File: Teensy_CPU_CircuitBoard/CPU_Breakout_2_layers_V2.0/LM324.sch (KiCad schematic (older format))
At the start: 44 parts

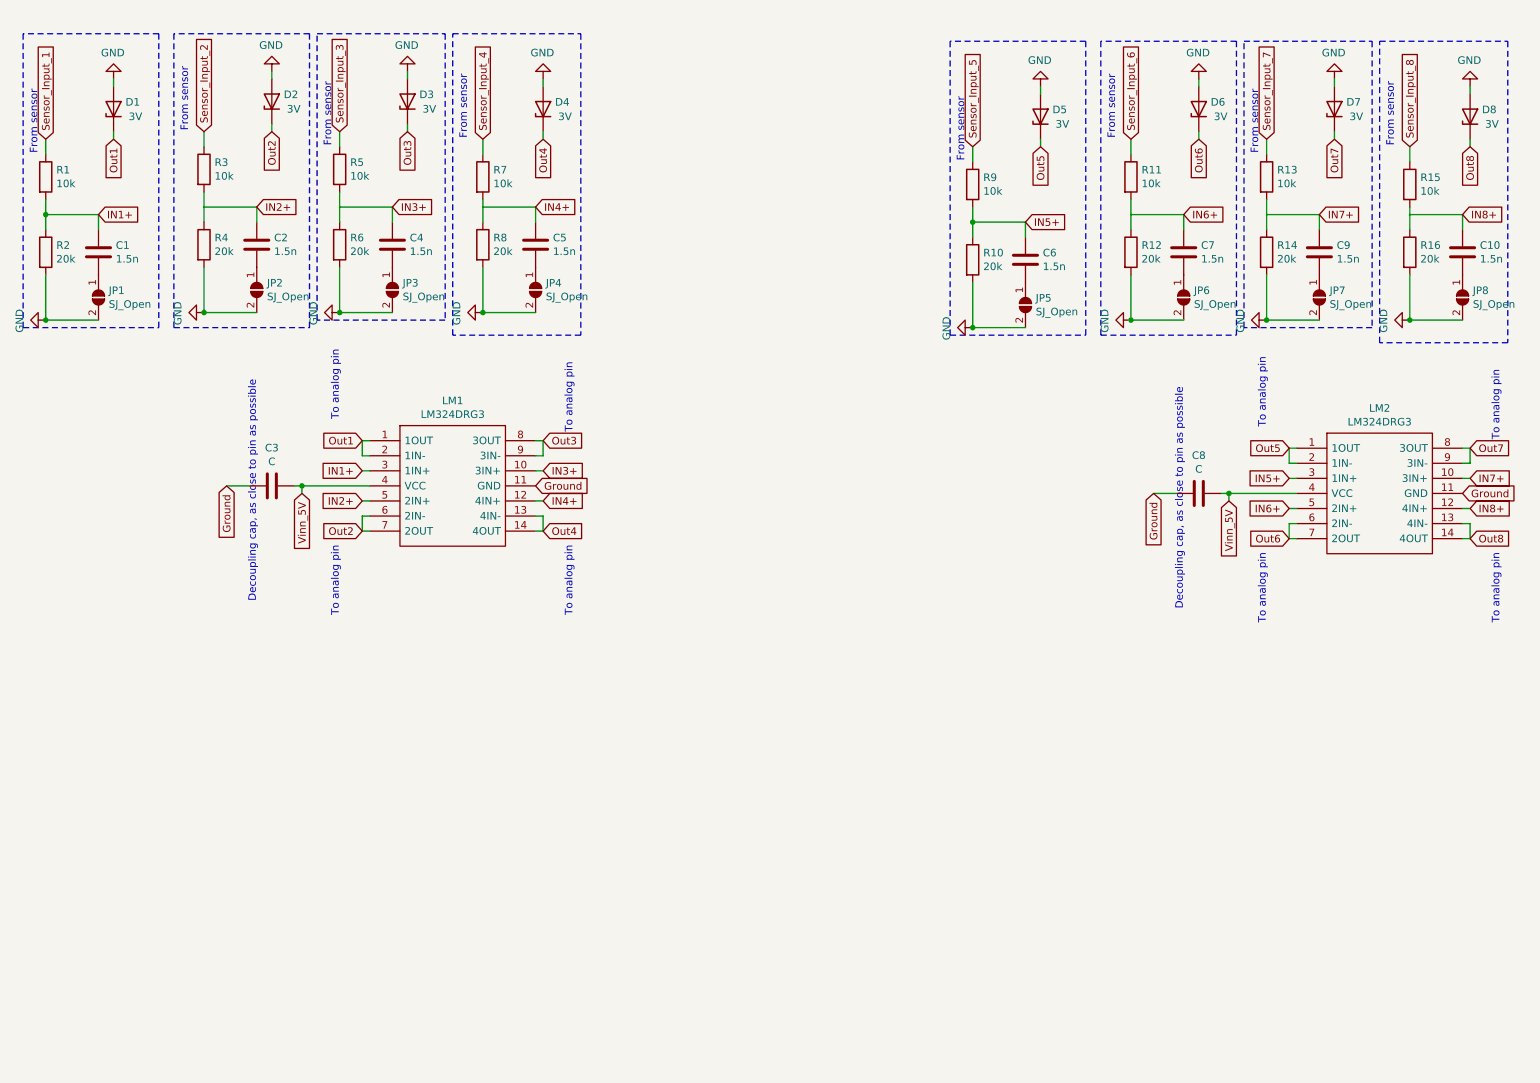
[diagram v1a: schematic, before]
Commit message: Suspension disp senson schematic done
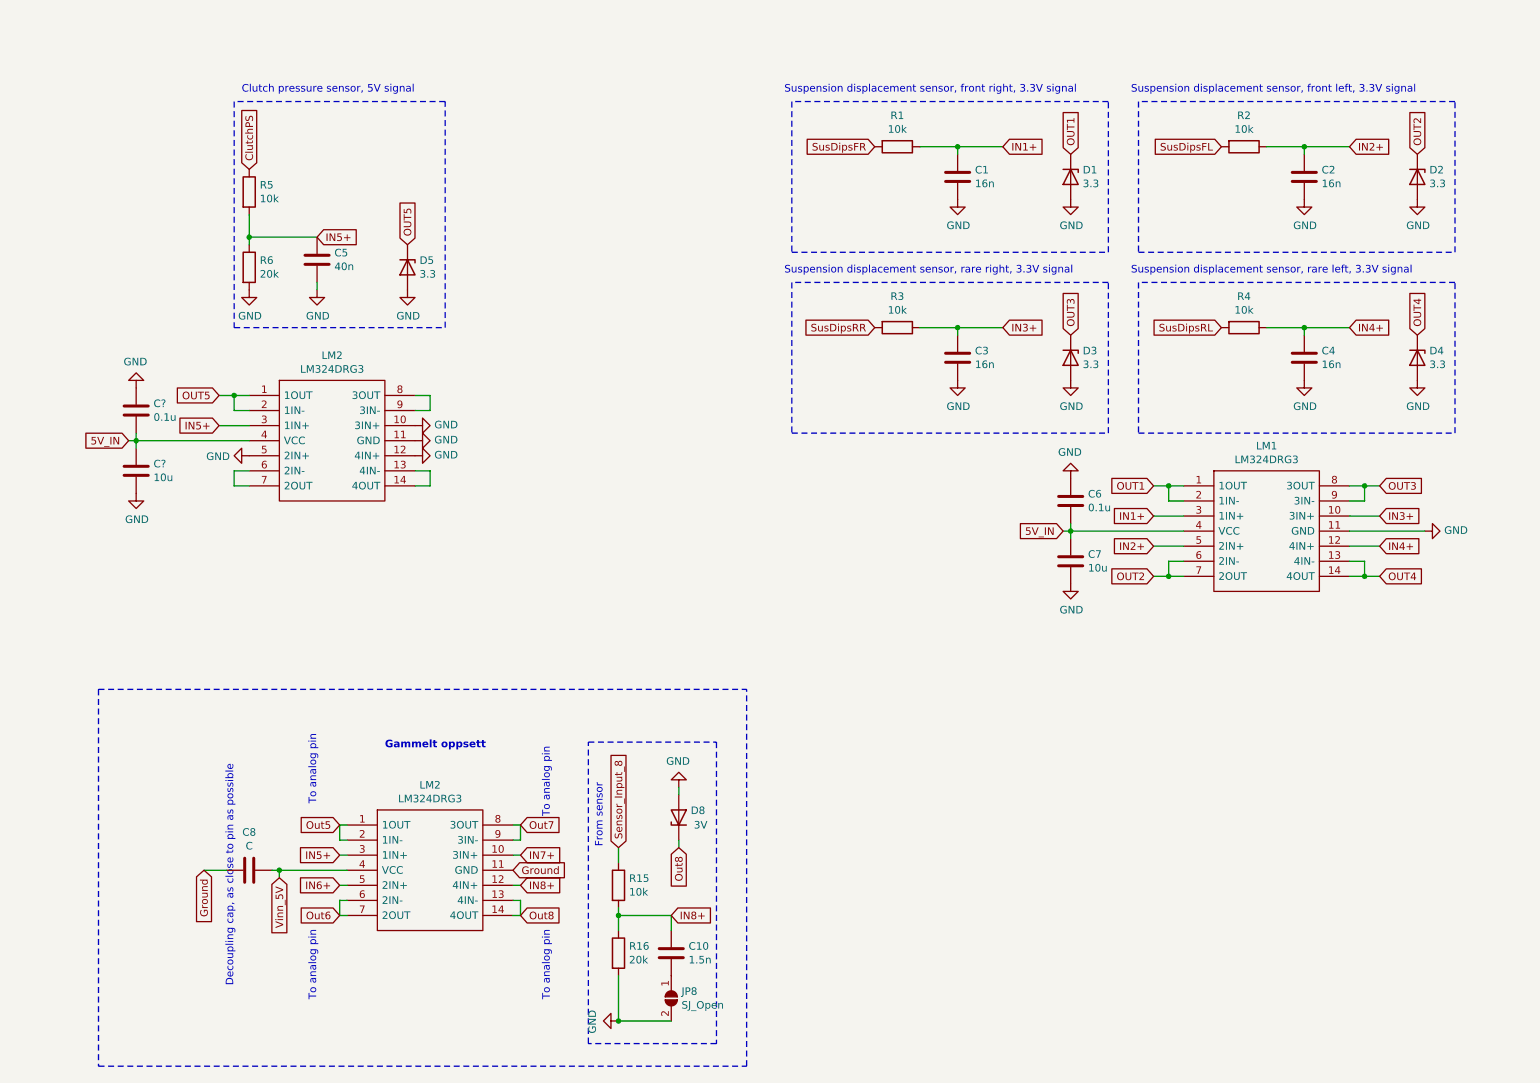
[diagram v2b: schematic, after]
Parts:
- removed C9: 1.5n, Capacitor_SMD:C_0603_1608Metric, symbol Device:C
- removed D6, D7: 3V, Diode_SMD:D_0603_1608Metric, symbol Device:D_Zener
- removed JP1, JP2, JP3, JP4, JP5, JP6, JP7: SJ_Open, Jumper:SolderJumper-2_P1.3mm_Open_RoundedPad1.0x1.5mm, symbol Jumper:SolderJumper_2_Open
- removed R10, R12, R14, R8: 20k, Resistor_SMD:R_0603_1608Metric, symbol Device:R
- removed R11, R13, R7, R9: 10k, Resistor_SMD:R_0603_1608Metric, symbol Device:R
- added C?: 10u, Capacitor_SMD:C_0603_1608Metric, symbol Device:C
- added C?: 0.1u, Capacitor_SMD:C_0603_1608Metric, symbol Device:C
- added LM2: LM324DRG3, Package_SO:SOIC-14_3.9x8.7mm_P1.27mm, symbol BreakoutBoardTeensy:LM324DRG3
- C1, C2, C4: value 1.5n -> 16n
- C3: value C -> 16n
- C5: value 1.5n -> 40n
- C6: value 1.5n -> 0.1u
- C7: value 1.5n -> 10u
- D1, D2, D3, D4, D5: value 3V -> 3.3
- R2, R4: value 20k -> 10k
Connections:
- net Sensor_Input_1 is gone; now on net IN1+: R1.1
- net Sensor_Input_2 is gone; now on net IN3+: R3.1
- net GND: now also C1.2, C2.2, C3.2, C4.2, C5.2, C6.1, C7.2, LM1.11 (GND), C?.1, C?.2, LM2.10 (3IN+), LM2.11 (GND), LM2.12 (4IN+), LM2.5 (2IN+); no longer R2.2, R4.2
- net Ground: no longer C3.1, LM1.11 (GND)
- net IN1+: no longer R1.2, R2.1
- net IN2+: now also R2.1; no longer R3.2, R4.1
- net IN3+: now also C3.1; no longer C4.1, R5.2, R6.1
- net IN4+: now also C4.1, R4.1; no longer C5.1
- net IN5+: now also C5.1, R5.2, R6.1, LM2.3 (1IN+); no longer C6.1
- net IN6+: no longer C7.1
- net Out5: no longer D5.1 (K)
- net Vinn_5V: no longer C3.2, LM1.4 (VCC)
- net 5V_IN: now reaches C6.2
- net 5V_IN: now also C7.1, LM1.4 (VCC), C?.1, C?.2, LM2.4 (VCC)
- net Out1 renamed OUT1
- net Out2 renamed OUT2
- net Out3 renamed OUT3
- net Out4 renamed OUT4
- net Sensor_Input_3 renamed ClutchPS
- new net: LM2.13 (4IN-), LM2.14 (4OUT)
- new net: LM2.6 (2IN-), LM2.7 (2OUT)
- new net: LM2.8 (3OUT), LM2.9 (3IN-)
- new net OUT5: D5.1 (K), LM2.1 (1OUT), LM2.2 (1IN-)
- new net SusDipsFL: R2.2
- new net SusDipsFR: R1.2
- new net SusDipsRL: R4.2
- new net SusDipsRR: R3.2
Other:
- note added: "Clutch pressure sensor, 5V signal\n"
- note added: "Gammelt oppsett"
- note added: "Suspension displacement sensor, front left, 3.3V signal"
- note added: "Suspension displacement sensor, front right, 3.3V signal"
- note added: "Suspension displacement sensor, rare left, 3.3V signal"
- note added: "Suspension displacement sensor, rare right, 3.3V signal"
- moved on the sheet: C10, C8, D8, JP8, LM1, LM2, R15, R16

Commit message: Added footprints diodes ++
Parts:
- removed C10: 1.5n, Capacitor_SMD:C_0603_1608Metric, symbol Device:C
- removed C6, C?: 0.1u, Capacitor_SMD:C_0603_1608Metric, symbol Device:C
- removed C7, C?: 10u, Capacitor_SMD:C_0603_1608Metric, symbol Device:C
- removed C8: C, Capacitor_SMD:C_0603_1608Metric, symbol Device:C
- removed D1, D2, D3, D4, D5: 3.3, Diode_SMD:D_0603_1608Metric, symbol Device:D_Zener
- removed D8: 3V, Diode_SMD:D_0603_1608Metric, symbol Device:D_Zener
- removed JP8: SJ_Open, Jumper:SolderJumper-2_P1.3mm_Open_RoundedPad1.0x1.5mm, symbol Jumper:SolderJumper_2_Open
- removed LM1, LM2 (x2): LM324DRG3, Package_SO:SOIC-14_3.9x8.7mm_P1.27mm, symbol BreakoutBoardTeensy:LM324DRG3
- removed R15: 10k, Resistor_SMD:R_0603_1608Metric, symbol Device:R
- removed R16: 20k, Resistor_SMD:R_0603_1608Metric, symbol Device:R
- added D6, D? (x4): D_Zener_MM3Z3V6T1G, Teensy_Footprint_Library:D_0603_MM3Z3V6T1G, symbol teensy4_header_breakout-cache:D_Zener_MM3Z3V6T1G
- C5: value 40n -> 15n
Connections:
- net GND: now also D6.2 (A), D?.2 (A), D?.2 (A), D?.2 (A), D?.2 (A)
- net IN1+: no longer names the net of C1.1, R1.1
- net IN1+: now also D?.1 (K)
- net IN2+: no longer names the net of C2.1, R2.1
- net IN2+: now also D?.1 (K)
- net IN3+: no longer names the net of C3.1, R3.1
- net IN3+: now also D?.1 (K)
- net IN4+: no longer names the net of C4.1, R4.1
- net IN4+: now also D?.1 (K)
- net IN5+: no longer names the net of C5.1, R5.2, R6.1
- net IN5+: now also D6.1 (K)
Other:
- note removed: "Decoupling cap, as close to pin as possible\n"
- note removed: "From sensor"
- note removed: "Gammelt oppsett"
- note removed: "To analog pin"
- moved on the sheet: C1, C2, C3, C4, C5, R1, R2, R3, R4, R5, R6

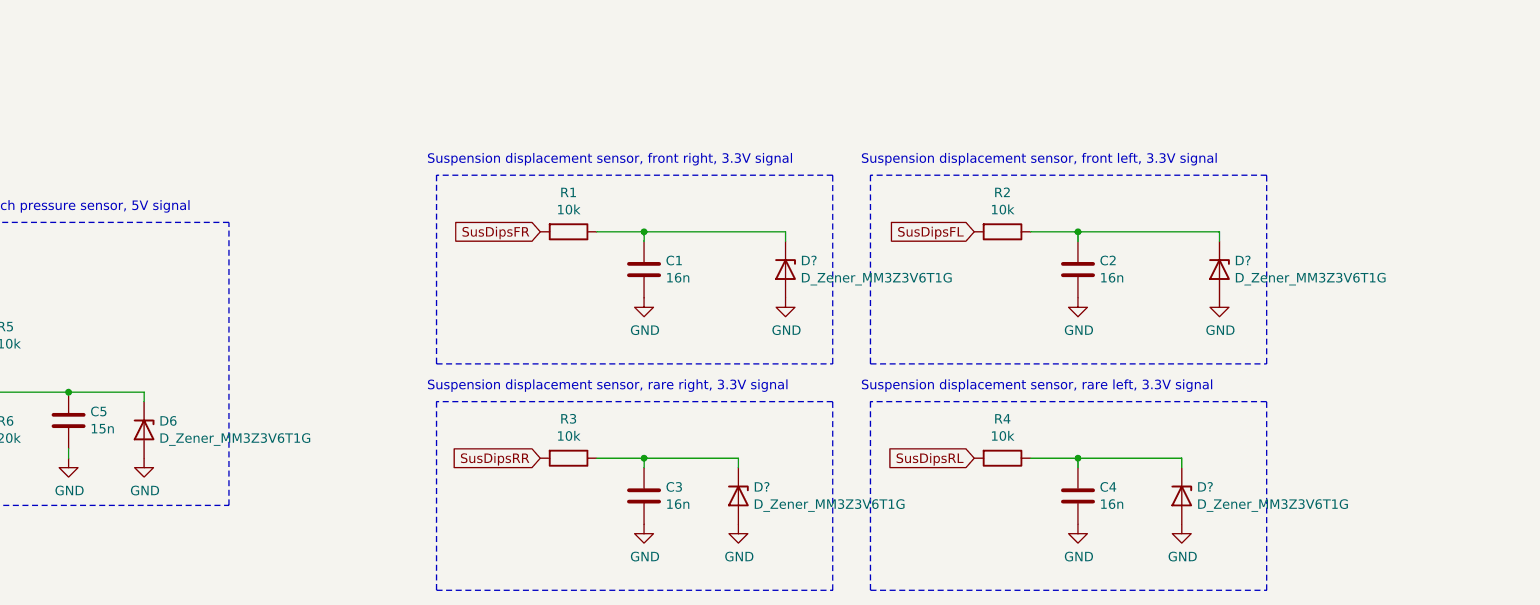
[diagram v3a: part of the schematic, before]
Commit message: Nearly completed schematics. Ready for tracing?
Short cleanup in footprint library
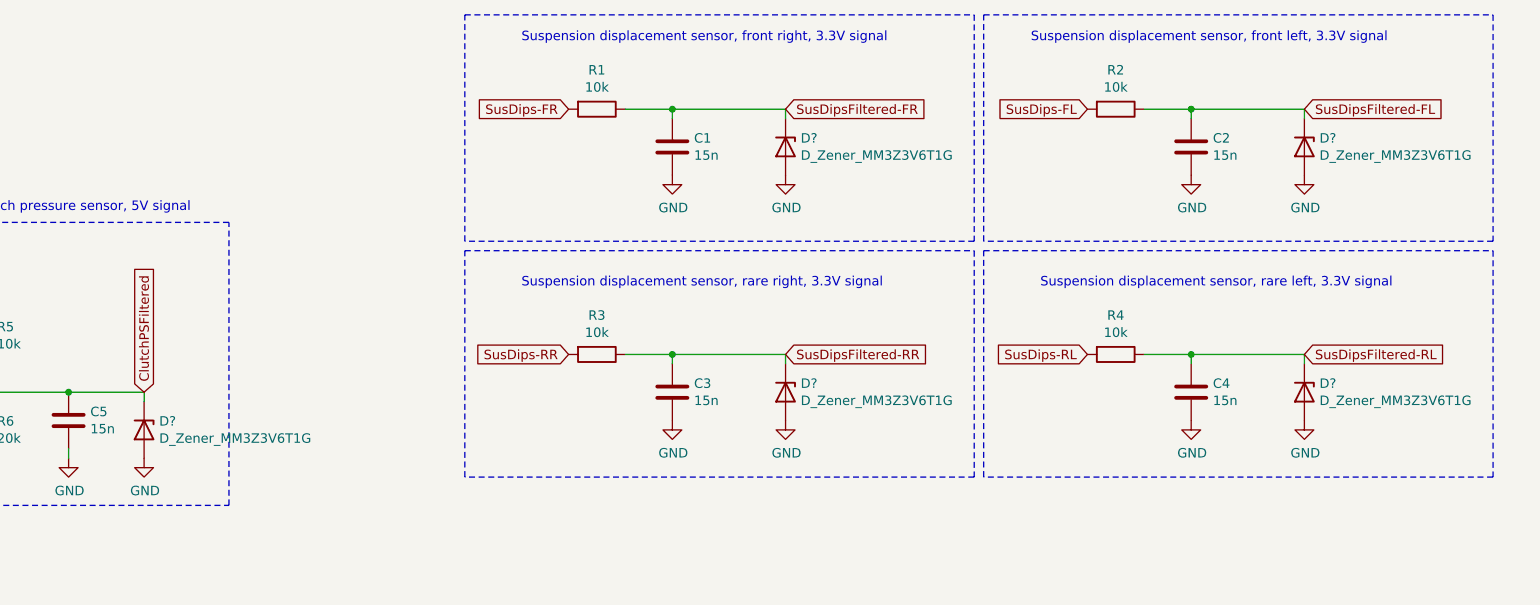
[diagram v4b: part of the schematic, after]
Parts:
- C1, C2, C3, C4: value 16n -> 15n
- renumbered D6 to D?
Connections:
- net ClutchPSFiltered: now reaches C5.1, D?.1 (K), R5.2, R6.1
- net SusDipsFiltered-FR: now reaches C1.1, D?.1 (K), R1.1
- net SusDipsFiltered-RR: now reaches C3.1, D?.1 (K), R3.1
- net SusDipsFiltered-RL: now reaches C4.1, D?.1 (K), R4.1
- net SusDipsFiltered-FL: now reaches C2.1, D?.1 (K), R2.1
- net SusDipsFL renamed SusDips-FL
- net SusDipsFR renamed SusDips-FR
- net SusDipsRL renamed SusDips-RL
- net SusDipsRR renamed SusDips-RR
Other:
- moved on the sheet: C1, C2, C3, C4, D?, R1, R2, R3, R4

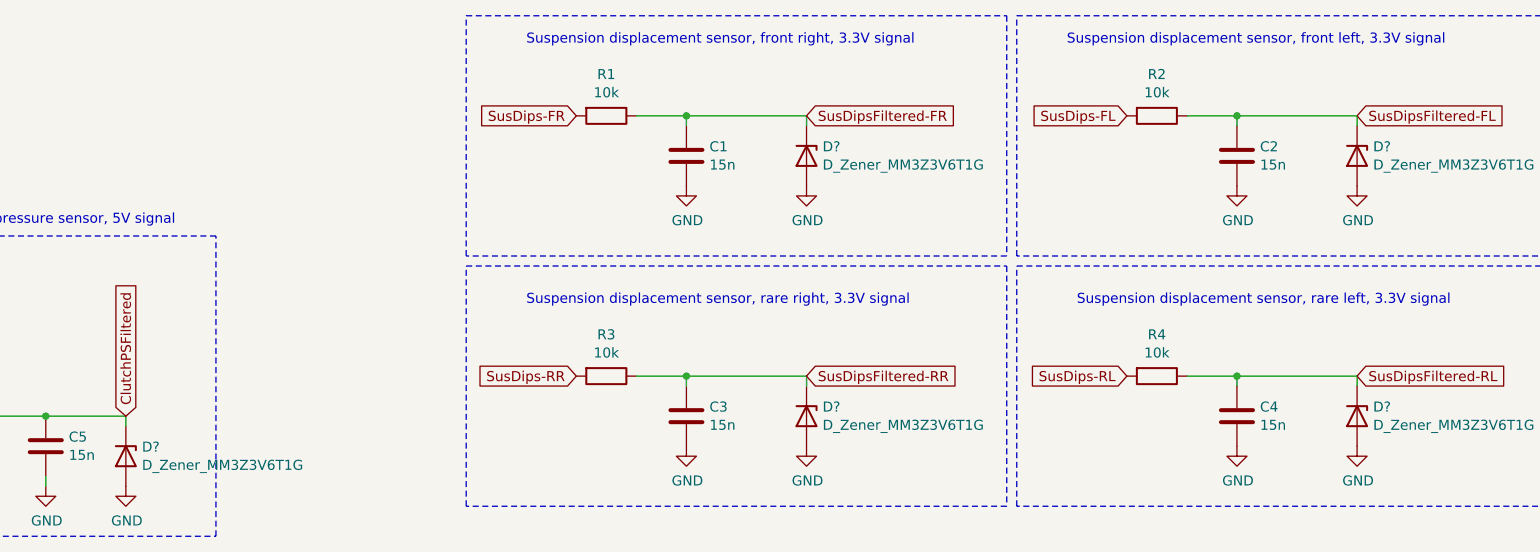
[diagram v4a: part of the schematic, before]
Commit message: PCB trace 1.0V
Har ikke lagt til spenningsforsyning til sensorene eller GND. Dessuten har jeg satt connectoren feil vei
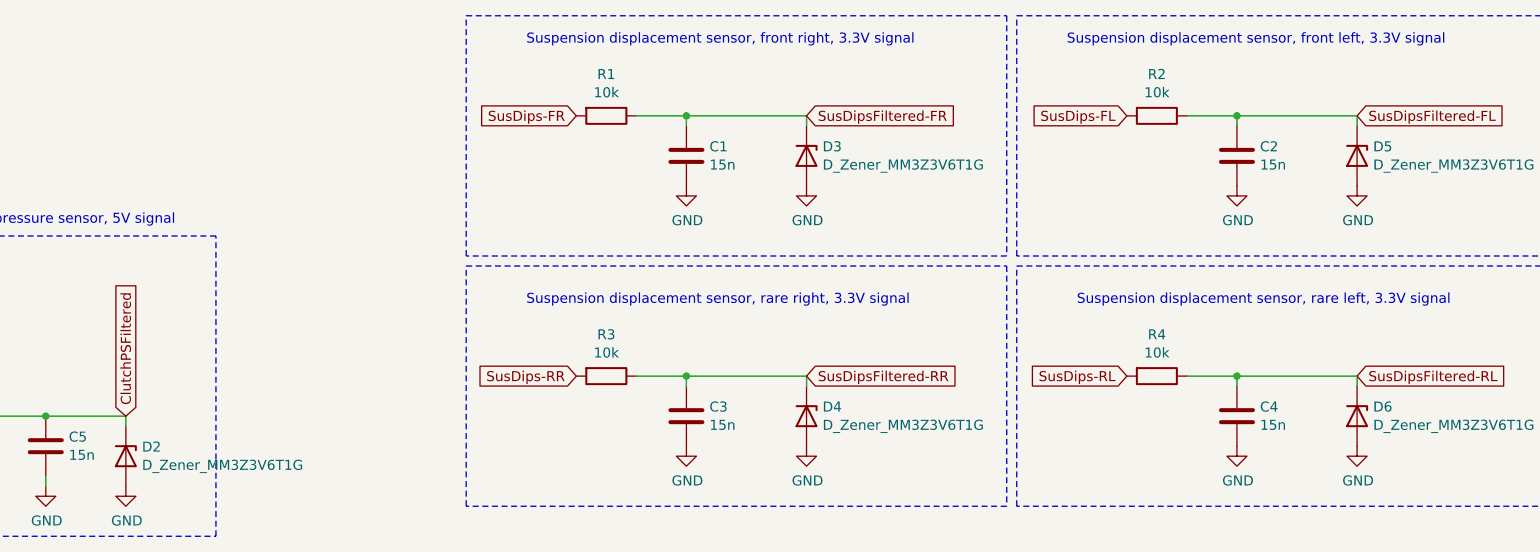
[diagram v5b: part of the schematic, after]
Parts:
- gave numbers to parts that had none: 5
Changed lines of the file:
@@
 	6450 2700 6450 2750
 $Comp
-L teensy4_header_breakout-cache:D_Zener_MM3Z3V6T1G D?
+L teensy4_header_breakout-cache:D_Zener_MM3Z3V6T1G D2
 U 1 1 5FE744BC
 P 3050 3100
-F 0 "D?" V 3004 3180 50  0000 L CNN
+F 0 "D2" V 3004 3180 50  0000 L CNN
 F 1 "D_Zener_MM3Z3V6T1G" V 3095 3180 50  0000 L CNN
 F 2 "Teensy_Footprint_Library:D_0603_MM3Z3V6T1G" H 3050 3100 50  0001 C CNN
@@
 $EndComp
 $Comp
-L teensy4_header_breakout-cache:D_Zener_MM3Z3V6T1G D?
+L teensy4_header_breakout-cache:D_Zener_MM3Z3V6T1G D3
 U 1 1 5FE76A9F
 P 6450 1600
-F 0 "D?" V 6404 1680 50  0000 L CNN
+F 0 "D3" V 6404 1680 50  0000 L CNN
 F 1 "D_Zener_MM3Z3V6T1G" V 6495 1680 50  0000 L CNN
 F 2 "Teensy_Footprint_Library:D_0603_MM3Z3V6T1G" H 6450 1600 50  0001 C CNN
@@
 $EndComp
 $Comp
-L teensy4_header_breakout-cache:D_Zener_MM3Z3V6T1G D?
+L teensy4_header_breakout-cache:D_Zener_MM3Z3V6T1G D4
 U 1 1 5FE7712F
 P 6450 2900
-F 0 "D?" V 6404 2980 50  0000 L CNN
+F 0 "D4" V 6404 2980 50  0000 L CNN
 F 1 "D_Zener_MM3Z3V6T1G" V 6495 2980 50  0000 L CNN
 F 2 "Teensy_Footprint_Library:D_0603_MM3Z3V6T1G" H 6450 2900 50  0001 C CNN
@@
 $EndComp
 $Comp
-L teensy4_header_breakout-cache:D_Zener_MM3Z3V6T1G D?
+L teensy4_header_breakout-cache:D_Zener_MM3Z3V6T1G D6
 U 1 1 5FE778C8
 P 9200 2900
-F 0 "D?" V 9154 2980 50  0000 L CNN
+F 0 "D6" V 9154 2980 50  0000 L CNN
 F 1 "D_Zener_MM3Z3V6T1G" V 9245 2980 50  0000 L CNN
 F 2 "Teensy_Footprint_Library:D_0603_MM3Z3V6T1G" H 9200 2900 50  0001 C CNN
@@
 $EndComp
 $Comp
-L teensy4_header_breakout-cache:D_Zener_MM3Z3V6T1G D?
+L teensy4_header_breakout-cache:D_Zener_MM3Z3V6T1G D5
 U 1 1 5FE77F85
 P 9200 1600
-F 0 "D?" V 9154 1680 50  0000 L CNN
+F 0 "D5" V 9154 1680 50  0000 L CNN
 F 1 "D_Zener_MM3Z3V6T1G" V 9245 1680 50  0000 L CNN
 F 2 "Teensy_Footprint_Library:D_0603_MM3Z3V6T1G" H 9200 1600 50  0001 C CNN

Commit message: Schematic DONE, started tracing
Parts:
- D2, D3, D4, D5, D6: footprint Teensy_Footprint_Library:D_0603_MM3Z3V6T1G -> Teensy_Footprint_Library:D_SOD-323-MM3Z3V6T1G
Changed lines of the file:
@@
 F 0 "D2" V 3004 3180 50  0000 L CNN
 F 1 "D_Zener_MM3Z3V6T1G" V 3095 3180 50  0000 L CNN
-F 2 "Teensy_Footprint_Library:D_0603_MM3Z3V6T1G" H 3050 3100 50  0001 C CNN
+F 2 "Teensy_Footprint_Library:D_SOD-323-MM3Z3V6T1G" H 3050 3100 50  0001 C CNN
 F 3 "~" H 3050 3100 50  0001 C CNN
 	1    3050 3100
@@
 F 0 "D3" V 6404 1680 50  0000 L CNN
 F 1 "D_Zener_MM3Z3V6T1G" V 6495 1680 50  0000 L CNN
-F 2 "Teensy_Footprint_Library:D_0603_MM3Z3V6T1G" H 6450 1600 50  0001 C CNN
+F 2 "Teensy_Footprint_Library:D_SOD-323-MM3Z3V6T1G" H 6450 1600 50  0001 C CNN
 F 3 "~" H 6450 1600 50  0001 C CNN
 	1    6450 1600
@@
 F 0 "D4" V 6404 2980 50  0000 L CNN
 F 1 "D_Zener_MM3Z3V6T1G" V 6495 2980 50  0000 L CNN
-F 2 "Teensy_Footprint_Library:D_0603_MM3Z3V6T1G" H 6450 2900 50  0001 C CNN
+F 2 "Teensy_Footprint_Library:D_SOD-323-MM3Z3V6T1G" H 6450 2900 50  0001 C CNN
 F 3 "~" H 6450 2900 50  0001 C CNN
 	1    6450 2900
@@
 F 0 "D6" V 9154 2980 50  0000 L CNN
 F 1 "D_Zener_MM3Z3V6T1G" V 9245 2980 50  0000 L CNN
-F 2 "Teensy_Footprint_Library:D_0603_MM3Z3V6T1G" H 9200 2900 50  0001 C CNN
+F 2 "Teensy_Footprint_Library:D_SOD-323-MM3Z3V6T1G" H 9200 2900 50  0001 C CNN
 F 3 "~" H 9200 2900 50  0001 C CNN
 	1    9200 2900
@@
 F 0 "D5" V 9154 1680 50  0000 L CNN
 F 1 "D_Zener_MM3Z3V6T1G" V 9245 1680 50  0000 L CNN
-F 2 "Teensy_Footprint_Library:D_0603_MM3Z3V6T1G" H 9200 1600 50  0001 C CNN
+F 2 "Teensy_Footprint_Library:D_SOD-323-MM3Z3V6T1G" H 9200 1600 50  0001 C CNN
 F 3 "~" H 9200 1600 50  0001 C CNN
 	1    9200 1600
